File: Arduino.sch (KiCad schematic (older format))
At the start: 0 parts

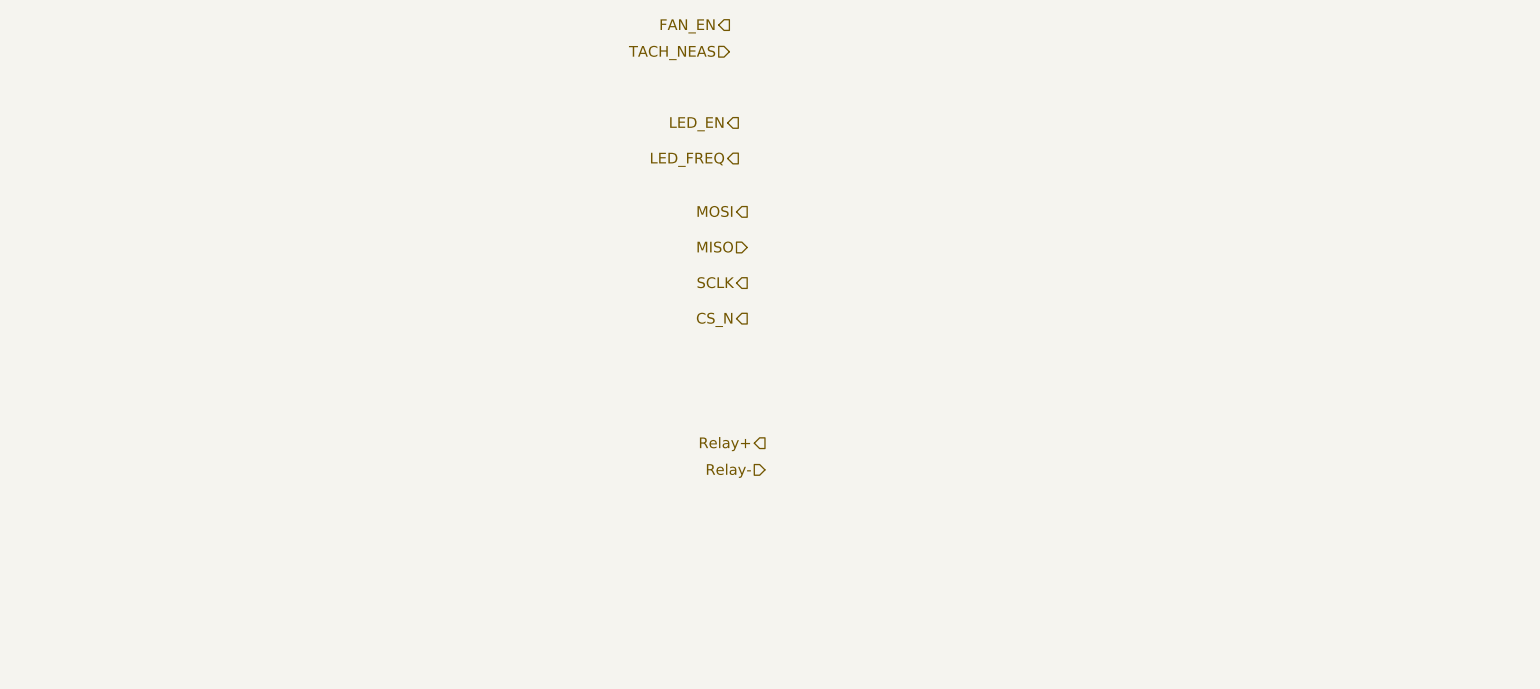
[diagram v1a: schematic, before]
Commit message: Struktur nach Arduino
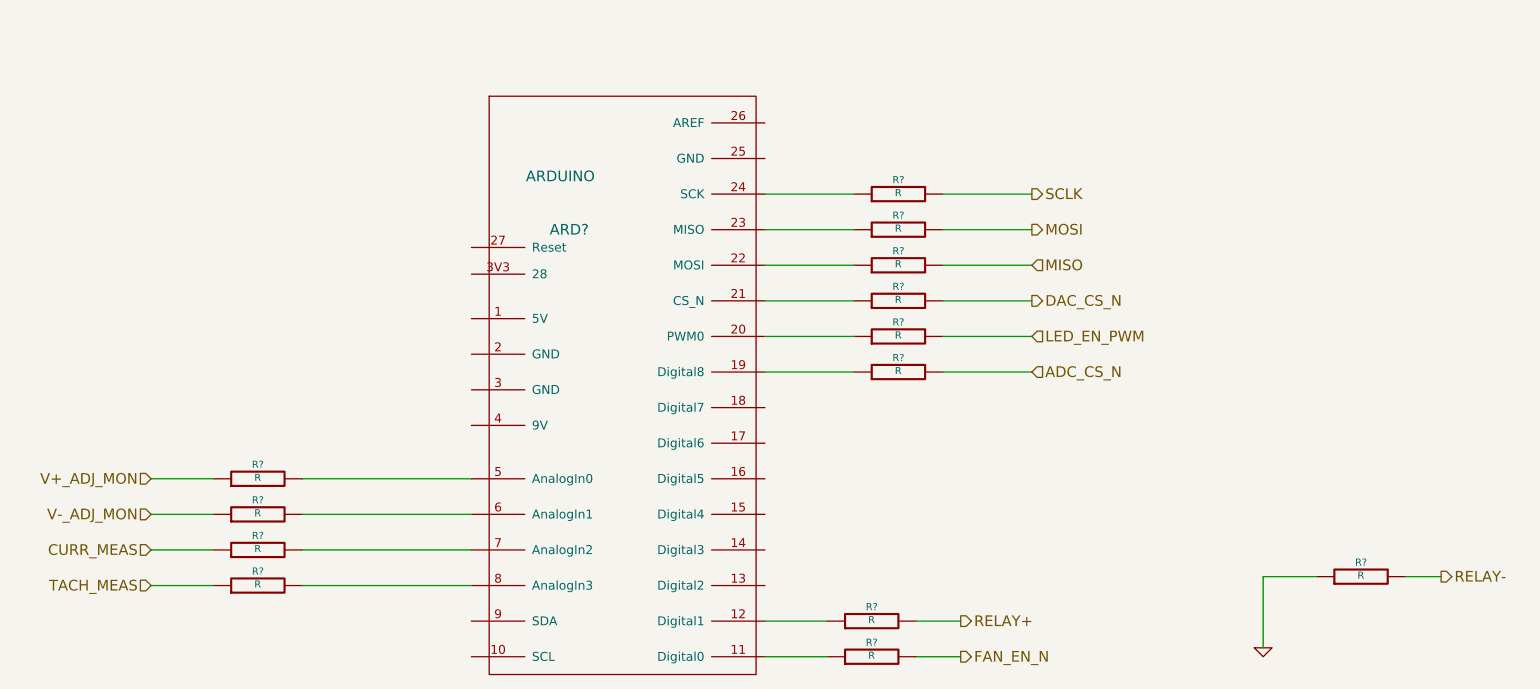
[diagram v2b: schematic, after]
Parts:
- added ARD?: ARDUINO, symbol ARDUINO
- added R? (x13): R, ~, symbol R
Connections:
- net MISO: now also R?.2
- net MOSI: now also R?.2
- net SCLK: now also R?.2
- new net: ARD?.11 (Digital0), R?.1
- new net: ARD?.12 (Digital1), R?.1
- new net: ARD?.19 (Digital8), R?.1
- new net: ARD?.20 (PWM0), R?.1
- new net: ARD?.21 (CS_N), R?.1
- new net: ARD?.22 (MOSI), R?.1
- new net: ARD?.23 (MISO), R?.1
- new net: ARD?.24 (SCK), R?.1
- new net: ARD?.5 (AnalogIn0), R?.2
- new net: ARD?.6 (AnalogIn1), R?.2
- new net: ARD?.7 (AnalogIn2), R?.2
- new net: ARD?.8 (AnalogIn3), R?.2
- new net ADC_CS_N: R?.2
- new net CURR_MEAS: R?.1
- new net DAC_CS_N: R?.2
- new net FAN_EN_N: R?.2
- new net GND: R?.1
- new net LED_EN_PWM: R?.2
- new net RELAY+: R?.2
- new net RELAY-: R?.2
- new net TACH_MEAS: R?.1
- new net V+_ADJ_MON: R?.1
- new net V-_ADJ_MON: R?.1

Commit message: Fan/Current Module Refactoring
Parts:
- added R? (x2): R, ~, symbol R
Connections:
- net at R?.1: now also ARD?.21 (CS_N); no longer ARD?.11 (Digital0)
- net at ARD?.18 (Digital7): now also R?.1
- net at ARD?.4 (9V): now also R?.2
- net FAN_EN_N renamed FAN_PWM
- new net: ARD?.11 (Digital0), R?.1
- new net +12P: R?.1
- new net FAN_MODE: R?.2
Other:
- moved on the sheet: R?
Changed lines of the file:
@@
 $Descr A4 11693 8268
 encoding utf-8
-Sheet 2 9
+Sheet 9 9
 Title ""
-Date "6 feb 2014"
+Date "7 feb 2014"
 Rev ""
 Comp ""
@@
 Comment4 ""
 $EndDescr
-Text HLabel 6750 4400 2    60   Output ~ 0
+Text HLabel 7100 4400 2    60   Output ~ 0
 RELAY+
 Text HLabel 9450 4150 2    60   Output ~ 0
@@
 Text HLabel 7150 2000 2    60   Output ~ 0
 SCLK
+Text HLabel 7100 3200 2    60   Output ~ 0
+DAC_CS_N
 Text HLabel 7150 2600 2    60   Output ~ 0
-DAC_CS_N
-Text HLabel 6750 4600 2    60   Output ~ 0
-FAN_EN_N
+FAN_PWM
 Text HLabel 2200 4200 0    60   Input ~ 0
 TACH_MEAS
@@
 L R R?
 U 1 1 52F2D1B0
-P 6250 4600
-F 0 "R?" V 6330 4600 40  0000 C CNN
-F 1 "R" V 6257 4601 40  0000 C CNN
-F 2 "~" V 6180 4600 30  0000 C CNN
-F 3 "~" H 6250 4600 30  0000 C CNN
-	1    6250 4600
+P 6400 2600
+F 0 "R?" V 6480 2600 40  0000 C CNN
+F 1 "R" V 6407 2601 40  0000 C CNN
+F 2 "~" V 6330 2600 30  0000 C CNN
+F 3 "~" H 6400 2600 30  0000 C CNN
+	1    6400 2600
 	0    -1   -1   0
 $EndComp
@@
 L R R?
 U 1 1 52F2D1CF
-P 6250 4400
-F 0 "R?" V 6330 4400 40  0000 C CNN
-F 1 "R" V 6257 4401 40  0000 C CNN
-F 2 "~" V 6180 4400 30  0000 C CNN
-F 3 "~" H 6250 4400 30  0000 C CNN
-	1    6250 4400
+P 6400 4400
+F 0 "R?" V 6480 4400 40  0000 C CNN
+F 1 "R" V 6407 4401 40  0000 C CNN
+F 2 "~" V 6330 4400 30  0000 C CNN
+F 3 "~" H 6400 4400 30  0000 C CNN
+	1    6400 4400
 	0    -1   -1   0
 $EndComp
@@
 L R R?
 U 1 1 52F349E0
-P 6400 2600
-F 0 "R?" V 6480 2600 40  0000 C CNN
-F 1 "R" V 6407 2601 40  0000 C CNN
-F 2 "~" V 6330 2600 30  0000 C CNN
-F 3 "~" H 6400 2600 30  0000 C CNN
-	1    6400 2600
-	0    -1   -1   0
-$EndComp
-Wire Wire Line
-	6000 4400 5650 4400
-Wire Wire Line
-	6750 4400 6500 4400
-Wire Wire Line
-	6750 4600 6500 4600
-Wire Wire Line
-	6000 4600 5650 4600
+P 6400 3200
+F 0 "R?" V 6480 3200 40  0000 C CNN
+F 1 "R" V 6407 3201 40  0000 C CNN
+F 2 "~" V 6330 3200 30  0000 C CNN
+F 3 "~" H 6400 3200 30  0000 C CNN
+	1    6400 3200
+	0    -1   -1   0
+$EndComp
 Wire Wire Line
 	2200 4000 2550 4000
@@
 	5650 2400 6150 2400
 Wire Wire Line
-	6150 2600 5650 2600
-Wire Wire Line
 	6650 2000 7150 2000
 Wire Wire Line
@@
 Wire Wire Line
 	6650 2400 7150 2400
-Wire Wire Line
-	7150 2600 6650 2600
 $Comp
 L R R?
@@
 Wire Wire Line
 	6150 3000 5650 3000
+Wire Wire Line
+	6150 3200 5650 3200
+Wire Wire Line
+	6150 2600 5650 2600
+Wire Wire Line
+	7150 2600 6650 2600
+Text HLabel 7100 4600 2    60   Input ~ 0
+FAN_MODE
+$Comp
+L R R?
+U 1 1 52F52688
+P 6400 4600
+F 0 "R?" V 6480 4600 40  0000 C CNN
+F 1 "R" V 6407 4601 40  0000 C CNN
+F 2 "~" V 6330 4600 30  0000 C CNN
+F 3 "~" H 6400 4600 30  0000 C CNN
+	1    6400 4600
+	0    -1   -1   0
+$EndComp
+Wire Wire Line
+	7100 4600 6650 4600
+Wire Wire Line
+	6150 4600 5650 4600
+Wire Wire Line
+	6650 3200 7100 3200
+Wire Wire Line
+	7100 4400 6650 4400
+Wire Wire Line
+	6150 4400 5650 4400
+$Comp
+L R R?
+U 1 1 52F52781
+P 2800 3300
+F 0 "R?" V 2880 3300 40  0000 C CNN
+F 1 "R" V 2807 3301 40  0000 C CNN
+F 2 "~" V 2730 3300 30  0000 C CNN
+F 3 "~" H 2800 3300 30  0000 C CNN
+	1    2800 3300
+	0    -1   -1   0
+$EndComp
+$Comp
+L +12P #PWR?
+U 1 1 52F52793
+P 2200 3100
+F 0 "#PWR?" H 2200 3070 30  0001 C CNN
+F 1 "+12P" H 2200 3200 30  0000 C CNN
+F 2 "" H 2200 3100 60  0000 C CNN
+F 3 "" H 2200 3100 60  0000 C CNN
+	1    2200 3100
+	1    0    0    -1
+$EndComp
+Wire Wire Line
+	2200 3100 2200 3300
+Wire Wire Line
+	2200 3300 2550 3300
+Wire Wire Line
+	3050 3300 4000 3300
 $EndSCHEMATC

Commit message: Am Ende der 4. Woche
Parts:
- added R? (x3): R, ~, symbol R
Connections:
- net GND: now also R?.1, R?.1
- net at ARD?.1 (5V): now also R?.2
- net at ARD?.2 (GND): now also R?.2
- net at ARD?.3 (GND): now also R?.2
- new net +5V: R?.1
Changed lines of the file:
@@
 Sheet 9 9
 Title ""
-Date "7 feb 2014"
+Date "14 feb 2014"
 Rev ""
 Comp ""
@@
 L +12P #PWR?
 U 1 1 52F52793
-P 2200 3100
-F 0 "#PWR?" H 2200 3070 30  0001 C CNN
-F 1 "+12P" H 2200 3200 30  0000 C CNN
-F 2 "" H 2200 3100 60  0000 C CNN
-F 3 "" H 2200 3100 60  0000 C CNN
-	1    2200 3100
-	1    0    0    -1
-$EndComp
-Wire Wire Line
-	2200 3100 2200 3300
-Wire Wire Line
-	2200 3300 2550 3300
+P 1500 3100
+F 0 "#PWR?" H 1500 3070 30  0001 C CNN
+F 1 "+12P" H 1500 3200 30  0000 C CNN
+F 2 "" H 1500 3100 60  0000 C CNN
+F 3 "" H 1500 3100 60  0000 C CNN
+	1    1500 3100
+	1    0    0    -1
+$EndComp
 Wire Wire Line
 	3050 3300 4000 3300
+$Comp
+L R R?
+U 1 1 52FBCC0A
+P 2800 3100
+F 0 "R?" V 2880 3100 40  0000 C CNN
+F 1 "R" V 2807 3101 40  0000 C CNN
+F 2 "~" V 2730 3100 30  0000 C CNN
+F 3 "~" H 2800 3100 30  0000 C CNN
+	1    2800 3100
+	0    -1   -1   0
+$EndComp
+$Comp
+L R R?
+U 1 1 52FBCC10
+P 2800 2900
+F 0 "R?" V 2880 2900 40  0000 C CNN
+F 1 "R" V 2807 2901 40  0000 C CNN
+F 2 "~" V 2730 2900 30  0000 C CNN
+F 3 "~" H 2800 2900 30  0000 C CNN
+	1    2800 2900
+	0    -1   -1   0
+$EndComp
+$Comp
+L R R?
+U 1 1 52FBCC16
+P 2800 2700
+F 0 "R?" V 2880 2700 40  0000 C CNN
+F 1 "R" V 2807 2701 40  0000 C CNN
+F 2 "~" V 2730 2700 30  0000 C CNN
+F 3 "~" H 2800 2700 30  0000 C CNN
+	1    2800 2700
+	0    -1   -1   0
+$EndComp
+Wire Wire Line
+	3050 2700 4000 2700
+Wire Wire Line
+	3050 2900 4000 2900
+Wire Wire Line
+	3050 3100 4000 3100
+Wire Wire Line
+	2550 3300 1500 3300
+Wire Wire Line
+	1500 3300 1500 3100
+$Comp
+L GND #PWR?
+U 1 1 52FBCCAB
+P 1700 3200
+F 0 "#PWR?" H 1700 3200 30  0001 C CNN
+F 1 "GND" H 1700 3130 30  0001 C CNN
+F 2 "" H 1700 3200 60  0000 C CNN
+F 3 "" H 1700 3200 60  0000 C CNN
+	1    1700 3200
+	1    0    0    -1
+$EndComp
+$Comp
+L +5V #PWR?
+U 1 1 52FBCCBA
+P 1500 2450
+F 0 "#PWR?" H 1500 2540 20  0001 C CNN
+F 1 "+5V" H 1500 2540 30  0000 C CNN
+F 2 "" H 1500 2450 60  0000 C CNN
+F 3 "" H 1500 2450 60  0000 C CNN
+	1    1500 2450
+	1    0    0    -1
+$EndComp
+Wire Wire Line
+	2550 2700 1500 2700
+Wire Wire Line
+	1500 2700 1500 2450
+Wire Wire Line
+	2550 2900 1700 2900
+Wire Wire Line
+	1700 2900 1700 3200
+Wire Wire Line
+	2200 2900 2200 3100
+Wire Wire Line
+	2200 3100 2550 3100
+Connection ~ 2200 2900
 $EndSCHEMATC

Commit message: Nach Einfuegen Relay-Modul
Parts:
- gave numbers to parts that had none: 19
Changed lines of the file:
@@
 Sheet 9 9
 Title ""
-Date "14 feb 2014"
+Date "17 feb 2014"
 Rev ""
 Comp ""
@@
 CURR_MEAS
 $Comp
-L R R?
+L R R37
 U 1 1 52F2D1B0
 P 6400 2600
-F 0 "R?" V 6480 2600 40  0000 C CNN
+F 0 "R37" V 6480 2600 40  0000 C CNN
 F 1 "R" V 6407 2601 40  0000 C CNN
 F 2 "~" V 6330 2600 30  0000 C CNN
@@
 $EndComp
 $Comp
-L R R?
+L R R41
 U 1 1 52F2D1CF
 P 6400 4400
-F 0 "R?" V 6480 4400 40  0000 C CNN
+F 0 "R41" V 6480 4400 40  0000 C CNN
 F 1 "R" V 6407 4401 40  0000 C CNN
 F 2 "~" V 6330 4400 30  0000 C CNN
@@
 $EndComp
 $Comp
-L ARDUINO ARD?
+L ARDUINO ARD1
 U 1 1 52F2DB36
 P 4800 3150
-F 0 "ARD?" H 4550 4100 60  0000 C CNN
+F 0 "ARD1" H 4550 4100 60  0000 C CNN
 F 1 "ARDUINO" H 4500 4400 60  0000 C CNN
 F 2 "" H 4800 3150 60  0000 C CNN
@@
 $EndComp
 $Comp
-L GND #PWR?
+L GND #PWR57
 U 1 1 52F3429E
 P 8450 4550
-F 0 "#PWR?" H 8450 4550 30  0001 C CNN
+F 0 "#PWR57" H 8450 4550 30  0001 C CNN
 F 1 "GND" H 8450 4480 30  0001 C CNN
 F 2 "" H 8450 4550 60  0000 C CNN
@@
 $EndComp
 $Comp
-L R R?
+L R R32
 U 1 1 52F342C5
 P 2800 4000
-F 0 "R?" V 2880 4000 40  0000 C CNN
+F 0 "R32" V 2880 4000 40  0000 C CNN
 F 1 "R" V 2807 4001 40  0000 C CNN
 F 2 "~" V 2730 4000 30  0000 C CNN
@@
 $EndComp
 $Comp
-L R R?
+L R R33
 U 1 1 52F342D2
 P 2800 4200
-F 0 "R?" V 2880 4200 40  0000 C CNN
+F 0 "R33" V 2880 4200 40  0000 C CNN
 F 1 "R" V 2807 4201 40  0000 C CNN
 F 2 "~" V 2730 4200 30  0000 C CNN
@@
 V-_ADJ_MON
 $Comp
-L R R?
+L R R31
 U 1 1 52F34941
 P 2800 3800
-F 0 "R?" V 2880 3800 40  0000 C CNN
+F 0 "R31" V 2880 3800 40  0000 C CNN
 F 1 "R" V 2807 3801 40  0000 C CNN
 F 2 "~" V 2730 3800 30  0000 C CNN
@@
 $EndComp
 $Comp
-L R R?
+L R R30
 U 1 1 52F34947
 P 2800 3600
-F 0 "R?" V 2880 3600 40  0000 C CNN
+F 0 "R30" V 2880 3600 40  0000 C CNN
 F 1 "R" V 2807 3601 40  0000 C CNN
 F 2 "~" V 2730 3600 30  0000 C CNN
@@
 $EndComp
 $Comp
-L R R?
+L R R34
 U 1 1 52F349C7
 P 6400 2000
-F 0 "R?" V 6480 2000 40  0000 C CNN
+F 0 "R34" V 6480 2000 40  0000 C CNN
 F 1 "R" V 6407 2001 40  0000 C CNN
 F 2 "~" V 6330 2000 30  0000 C CNN
@@
 $EndComp
 $Comp
-L R R?
+L R R35
 U 1 1 52F349D4
 P 6400 2200
-F 0 "R?" V 6480 2200 40  0000 C CNN
+F 0 "R35" V 6480 2200 40  0000 C CNN
 F 1 "R" V 6407 2201 40  0000 C CNN
 F 2 "~" V 6330 2200 30  0000 C CNN
@@
 $EndComp
 $Comp
-L R R?
+L R R36
 U 1 1 52F349DA
 P 6400 2400
-F 0 "R?" V 6480 2400 40  0000 C CNN
+F 0 "R36" V 6480 2400 40  0000 C CNN
 F 1 "R" V 6407 2401 40  0000 C CNN
 F 2 "~" V 6330 2400 30  0000 C CNN
@@
 $EndComp
 $Comp
-L R R?
+L R R40
 U 1 1 52F349E0
 P 6400 3200
-F 0 "R?" V 6480 3200 40  0000 C CNN
+F 0 "R40" V 6480 3200 40  0000 C CNN
 F 1 "R" V 6407 3201 40  0000 C CNN
 F 2 "~" V 6330 3200 30  0000 C CNN
@@
 	6650 2400 7150 2400
 $Comp
-L R R?
+L R R43
 U 1 1 52F34A8B
 P 9000 4150
-F 0 "R?" V 9080 4150 40  0000 C CNN
+F 0 "R43" V 9080 4150 40  0000 C CNN
 F 1 "R" V 9007 4151 40  0000 C CNN
 F 2 "~" V 8930 4150 30  0000 C CNN
@@
 	8450 4150 8450 4550
 $Comp
-L R R?
+L R R38
 U 1 1 52F34AC6
 P 6400 2800
-F 0 "R?" V 6480 2800 40  0000 C CNN
+F 0 "R38" V 6480 2800 40  0000 C CNN
 F 1 "R" V 6407 2801 40  0000 C CNN
 F 2 "~" V 6330 2800 30  0000 C CNN
@@
 	6150 2800 5650 2800
 $Comp
-L R R?
+L R R39
 U 1 1 52F3D8CD
 P 6400 3000
-F 0 "R?" V 6480 3000 40  0000 C CNN
+F 0 "R39" V 6480 3000 40  0000 C CNN
 F 1 "R" V 6407 3001 40  0000 C CNN
 F 2 "~" V 6330 3000 30  0000 C CNN
@@
 FAN_MODE
 $Comp
-L R R?
+L R R42
 U 1 1 52F52688
 P 6400 4600
-F 0 "R?" V 6480 4600 40  0000 C CNN
+F 0 "R42" V 6480 4600 40  0000 C CNN
 F 1 "R" V 6407 4601 40  0000 C CNN
 F 2 "~" V 6330 4600 30  0000 C CNN
@@
 	6150 4400 5650 4400
 $Comp
-L R R?
+L R R29
 U 1 1 52F52781
 P 2800 3300
-F 0 "R?" V 2880 3300 40  0000 C CNN
+F 0 "R29" V 2880 3300 40  0000 C CNN
 F 1 "R" V 2807 3301 40  0000 C CNN
 F 2 "~" V 2730 3300 30  0000 C CNN
@@
 $EndComp
 $Comp
-L +12P #PWR?
+L +12P #PWR55
 U 1 1 52F52793
 P 1500 3100
-F 0 "#PWR?" H 1500 3070 30  0001 C CNN
+F 0 "#PWR55" H 1500 3070 30  0001 C CNN
 F 1 "+12P" H 1500 3200 30  0000 C CNN
 F 2 "" H 1500 3100 60  0000 C CNN
@@
 	3050 3300 4000 3300
 $Comp
-L R R?
+L R R28
 U 1 1 52FBCC0A
 P 2800 3100
-F 0 "R?" V 2880 3100 40  0000 C CNN
+F 0 "R28" V 2880 3100 40  0000 C CNN
 F 1 "R" V 2807 3101 40  0000 C CNN
 F 2 "~" V 2730 3100 30  0000 C CNN
@@
 $EndComp
 $Comp
-L R R?
+L R R27
 U 1 1 52FBCC10
 P 2800 2900
-F 0 "R?" V 2880 2900 40  0000 C CNN
+F 0 "R27" V 2880 2900 40  0000 C CNN
 F 1 "R" V 2807 2901 40  0000 C CNN
 F 2 "~" V 2730 2900 30  0000 C CNN
@@
 $EndComp
 $Comp
-L R R?
+L R R26
 U 1 1 52FBCC16
 P 2800 2700
-F 0 "R?" V 2880 2700 40  0000 C CNN
+F 0 "R26" V 2880 2700 40  0000 C CNN
 F 1 "R" V 2807 2701 40  0000 C CNN
 F 2 "~" V 2730 2700 30  0000 C CNN
@@
 	1500 3300 1500 3100
 $Comp
-L GND #PWR?
+L GND #PWR56
 U 1 1 52FBCCAB
 P 1700 3200
-F 0 "#PWR?" H 1700 3200 30  0001 C CNN
+F 0 "#PWR56" H 1700 3200 30  0001 C CNN
 F 1 "GND" H 1700 3130 30  0001 C CNN
 F 2 "" H 1700 3200 60  0000 C CNN
@@
 $EndComp
 $Comp
-L +5V #PWR?
+L +5V #PWR54
 U 1 1 52FBCCBA
 P 1500 2450
-F 0 "#PWR?" H 1500 2540 20  0001 C CNN
+F 0 "#PWR54" H 1500 2540 20  0001 C CNN
 F 1 "+5V" H 1500 2540 30  0000 C CNN
 F 2 "" H 1500 2450 60  0000 C CNN

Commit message: Am Ende der 5. Woche.
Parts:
- added R46, R47, R50, R51: R, ~, symbol R
- ARD1: footprint (none) -> ~
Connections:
- net at ARD1.13 (Digital2): now also R51.1
- net at ARD1.14 (Digital3): now also R50.1
- net at ARD1.15 (Digital4): now also R47.1
- net at ARD1.16 (Digital5): now also R46.1
- net ADC_CS_N renamed ~ADC_CS
- net DAC_CS_N renamed ~DAC_CS
- new net ~DR: R47.2
- new net ~LDAC: R50.2
- new net ~RESET: R46.2
- new net ~SHDN: R51.2
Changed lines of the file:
@@
 Sheet 9 9
 Title ""
-Date "17 feb 2014"
+Date "22 feb 2014"
 Rev ""
 Comp ""
@@
 SCLK
 Text HLabel 7100 3200 2    60   Output ~ 0
-DAC_CS_N
+~DAC_CS
 Text HLabel 7150 2600 2    60   Output ~ 0
 FAN_PWM
@@
 $EndComp
 $Comp
-L ARDUINO ARD1
-U 1 1 52F2DB36
-P 4800 3150
-F 0 "ARD1" H 4550 4100 60  0000 C CNN
-F 1 "ARDUINO" H 4500 4400 60  0000 C CNN
-F 2 "" H 4800 3150 60  0000 C CNN
-F 3 "" H 4800 3150 60  0000 C CNN
-	1    4800 3150
-	1    0    0    -1
-$EndComp
-$Comp
-L GND #PWR57
+L GND #PWR062
 U 1 1 52F3429E
 P 8450 4550
-F 0 "#PWR57" H 8450 4550 30  0001 C CNN
+F 0 "#PWR062" H 8450 4550 30  0001 C CNN
 F 1 "GND" H 8450 4480 30  0001 C CNN
 F 2 "" H 8450 4550 60  0000 C CNN
@@
 $EndComp
 Text HLabel 7150 3000 2    60   Input ~ 0
-ADC_CS_N
+~ADC_CS
 Wire Wire Line
 	7150 3000 6650 3000
@@
 $EndComp
 $Comp
-L +12P #PWR55
+L +12P #PWR063
 U 1 1 52F52793
 P 1500 3100
-F 0 "#PWR55" H 1500 3070 30  0001 C CNN
+F 0 "#PWR063" H 1500 3070 30  0001 C CNN
 F 1 "+12P" H 1500 3200 30  0000 C CNN
 F 2 "" H 1500 3100 60  0000 C CNN
@@
 	1500 3300 1500 3100
 $Comp
-L GND #PWR56
+L GND #PWR064
 U 1 1 52FBCCAB
 P 1700 3200
-F 0 "#PWR56" H 1700 3200 30  0001 C CNN
+F 0 "#PWR064" H 1700 3200 30  0001 C CNN
 F 1 "GND" H 1700 3130 30  0001 C CNN
 F 2 "" H 1700 3200 60  0000 C CNN
@@
 $EndComp
 $Comp
-L +5V #PWR54
+L +5V #PWR065
 U 1 1 52FBCCBA
 P 1500 2450
-F 0 "#PWR54" H 1500 2540 20  0001 C CNN
+F 0 "#PWR065" H 1500 2540 20  0001 C CNN
 F 1 "+5V" H 1500 2540 30  0000 C CNN
 F 2 "" H 1500 2450 60  0000 C CNN
@@
 	2200 3100 2550 3100
 Connection ~ 2200 2900
+Text HLabel 7100 3600 2    60   Output ~ 0
+~RESET
+$Comp
+L R R46
+U 1 1 5303DF4C
+P 6400 3600
+F 0 "R46" V 6480 3600 40  0000 C CNN
+F 1 "R" V 6407 3601 40  0000 C CNN
+F 2 "~" V 6330 3600 30  0000 C CNN
+F 3 "~" H 6400 3600 30  0000 C CNN
+	1    6400 3600
+	0    -1   -1   0
+$EndComp
+Wire Wire Line
+	6150 3600 5650 3600
+Wire Wire Line
+	6650 3600 7100 3600
+Text HLabel 7100 3800 2    60   Output ~ 0
+~DR
+$Comp
+L R R47
+U 1 1 5303DF55
+P 6400 3800
+F 0 "R47" V 6480 3800 40  0000 C CNN
+F 1 "R" V 6407 3801 40  0000 C CNN
+F 2 "~" V 6330 3800 30  0000 C CNN
+F 3 "~" H 6400 3800 30  0000 C CNN
+	1    6400 3800
+	0    -1   -1   0
+$EndComp
+Wire Wire Line
+	6150 3800 5650 3800
+Wire Wire Line
+	6650 3800 7100 3800
+$Comp
+L ARDUINO ARD1
+U 1 1 5305CAD1
+P 4800 3150
+F 0 "ARD1" H 4550 4100 60  0000 C CNN
+F 1 "ARDUINO" H 4500 4400 60  0000 C CNN
+F 2 "~" H 4800 3150 60  0000 C CNN
+F 3 "~" H 4800 3150 60  0000 C CNN
+	1    4800 3150
+	1    0    0    -1
+$EndComp
+$Comp
+L R R50
+U 1 1 5305DC66
+P 6400 4000
+F 0 "R50" V 6480 4000 40  0000 C CNN
+F 1 "R" V 6407 4001 40  0000 C CNN
+F 2 "~" V 6330 4000 30  0000 C CNN
+F 3 "~" H 6400 4000 30  0000 C CNN
+	1    6400 4000
+	0    -1   -1   0
+$EndComp
+$Comp
+L R R51
+U 1 1 5305DC6C
+P 6400 4200
+F 0 "R51" V 6480 4200 40  0000 C CNN
+F 1 "R" V 6407 4201 40  0000 C CNN
+F 2 "~" V 6330 4200 30  0000 C CNN
+F 3 "~" H 6400 4200 30  0000 C CNN
+	1    6400 4200
+	0    -1   -1   0
+$EndComp
+Wire Wire Line
+	6150 4000 5650 4000
+Wire Wire Line
+	6150 4200 5650 4200
+Text HLabel 7100 4000 2    60   Input ~ 0
+~LDAC
+Wire Wire Line
+	7100 4000 6650 4000
+Text HLabel 7100 4200 2    60   Output ~ 0
+~SHDN
+Wire Wire Line
+	7100 4200 6650 4200
 $EndSCHEMATC
